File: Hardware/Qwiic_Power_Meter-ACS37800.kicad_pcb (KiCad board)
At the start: 4 copper layers, 30.5 x 38.1 mm, 55 parts, among them J1 Conn_01x01, J10 Conn_01x01, J11 Conn_01x01, J2 Conn_01x04, J3 Qwiic_RA, J4 HI, J5 LO, J6 Conn_01x01, J7 Qwiic_RA, J8 Conn_01x01, J9 Conn_01x01, U1 ACS37800

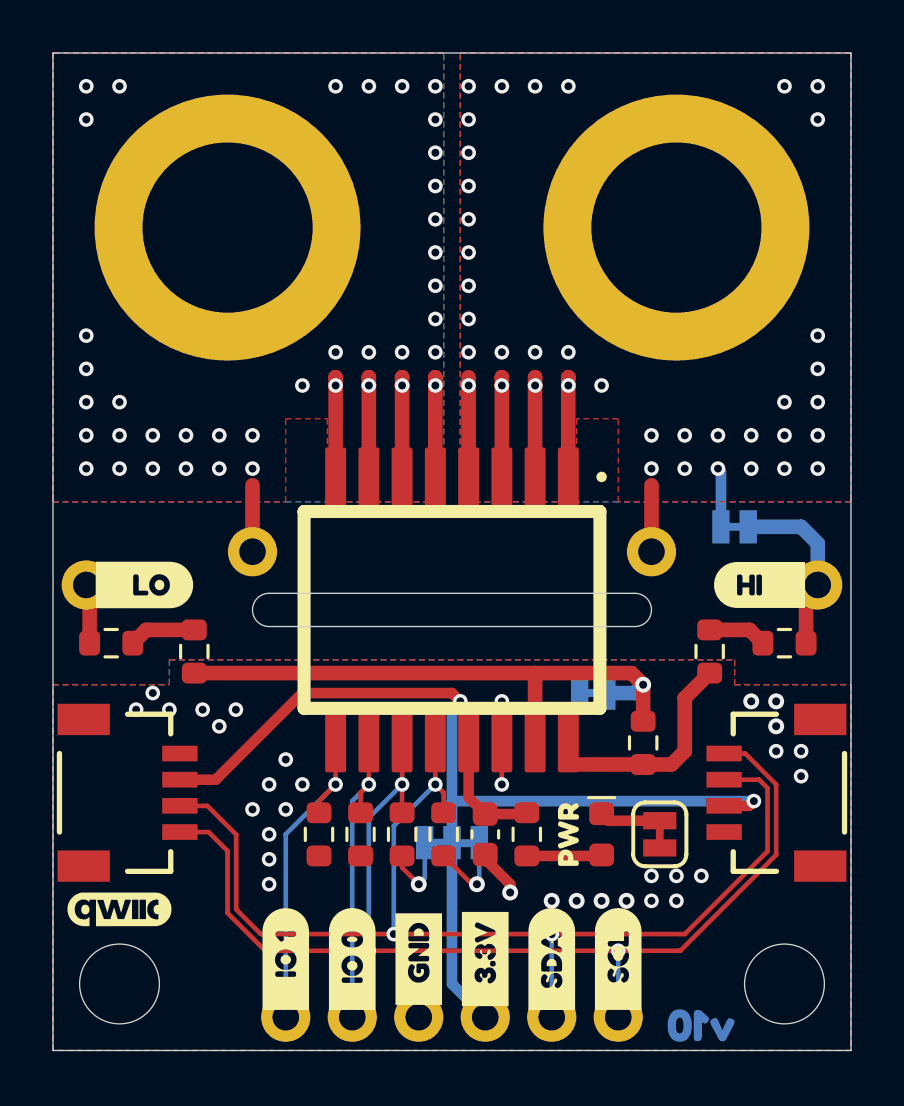
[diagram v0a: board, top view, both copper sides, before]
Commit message: Add missing fiducials
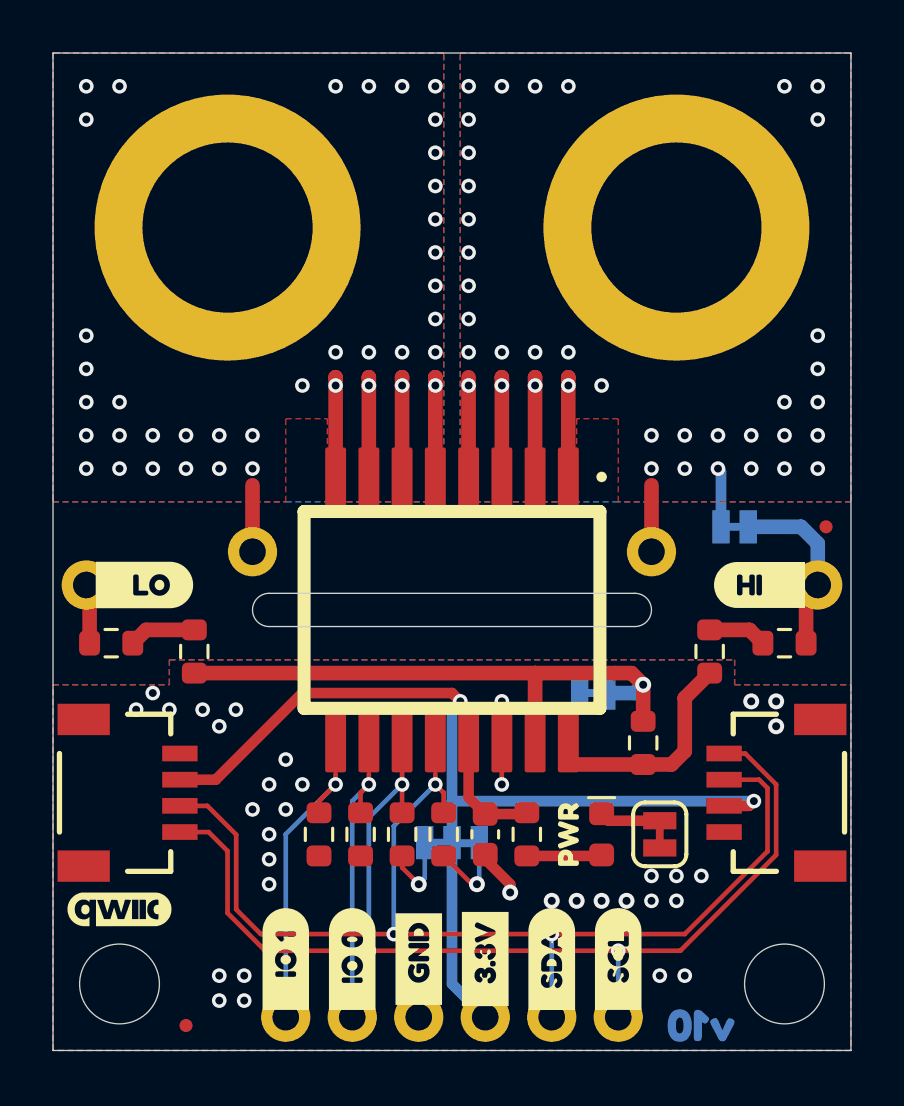
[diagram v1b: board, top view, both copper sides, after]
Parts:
- added Ref**: Fiducial_0.5mm_Mask1mm, SparkFun-Aesthetic:Fiducial_0.5mm_Mask1mm, F.Cu at (152.4, 95.9)
- added Ref**: Fiducial_0.5mm_Mask1mm, SparkFun-Aesthetic:Fiducial_0.5mm_Mask1mm, F.Cu at (128.0, 114.9)
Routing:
- net GND: vias 29 -> 35
- net (no net): vias 3 -> 0
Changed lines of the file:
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@@
 		(tags "kb_params=eyJBbGlnbm1lbnRDaG9pY2UiOiAiUmlnaHQiLCAiQ2FwTGVmdENob2ljZSI6ICJbIiwgIkNhcFJpZ2h0Q2hvaWNlIjogIl0iLCAiRm9udENvbWJvQm94IjogIkZyZWRkeVNwYXJrLVJlZ3VsYXIiLCAiSGVpZ2h0Q3RybCI6IDAuOCwgIkxheWVyQ29tYm9Cb3giOiAiRi5TaWxrUyIsICJMaW5lU3BhY2luZ0N0cmwiOiAxLjAsICJNdWx0aUxpbmVUZXh0IjogIlBXUiIsICJQYWRkaW5nQm90dG9tQ3RybCI6IDUuMCwgIlBhZGRpbmdMZWZ0Q3RybCI6IDUuMCwgIlBhZGRpbmdSaWdodEN0cmwiOiAwLjAsICJQYWRkaW5nVG9wQ3RybCI6IDUuMCwgIldpZHRoQ3RybCI6IDMuMCwgImFkdmFuY2VkQ2hlY2tib3giOiB0cnVlLCAiaW5saW5lRm9ybWF0VGV4dGJveCI6IHRydWUsICJsaW5lb3ZlclN0eWxlQ2hvaWNlIjogIlNxdWFyZSIsICJsaW5lb3ZlclRoaWNrbmVzc0N0cmwiOiAxfQ==")
 		(property "Reference" "kibuzzard-67B80BA2"
-			(at 0 -3.459445 270)
+			(at 0 -3.459445 -90)
 			(layer "F.SilkS")
 			(hide yes)
@@
 		)
 		(property "Value" "G***"
-			(at 0 3.459445 270)
+			(at 0 3.459445 -90)
 			(layer "F.SilkS")
 			(hide yes)
@@
 		)
 	)
+	(footprint "SparkFun-Aesthetic:Fiducial_0.5mm_Mask1mm"
+		(layer "F.Cu")
+		(at 152.4 95.885)
+		(descr "Circular Fiducial, 0.5mm bare copper, 1mm soldermask opening (Level C)")
+		(tags "SparkFun fiducial")
+		(property "Reference" "Ref**"
+			(at 0 -1.5 0)
+			(layer "F.Fab")
+			(effects
+				(font
+					(size 0.5 0.5)
+					(thickness 0.1)
+				)
+			)
+		)
+		(property "Value" "Fiducial_0.5mm_Mask1mm"
+			(at 0 1.5 0)
+			(layer "F.Fab")
+			(effects
+				(font
+					(size 0.5 0.5)
+					(thickness 0.1)
+				)
+			)
+		)
+		(property "Footprint" "SparkFun-Aesthetic:Fiducial_0.5mm_Mask1mm"
+			(at 0 0 0)
+			(unlocked yes)
+			(layer "F.Fab")
+			(hide yes)
+			(effects
+				(font
+					(size 1.27 1.27)
+				)
+			)
+		)
+		(property "Datasheet" ""
+			(at 0 0 0)
+			(unlocked yes)
+			(layer "F.Fab")
+			(hide yes)
+			(effects
+				(font
+					(size 1.27 1.27)
+				)
+			)
+		)
+		(property "Description" ""
+			(at 0 0 0)
+			(unlocked yes)
+			(layer "F.Fab")
+			(hide yes)
+			(effects
+				(font
+					(size 1.27 1.27)
+				)
+			)
+		)
+		(attr smd)
+		(fp_circle
+			(center 0 0)
+			(end 0.75 0)
+			(stroke
+				(width 0.05)
+				(type solid)
+			)
+			(fill none)
+			(layer "F.CrtYd")
+		)
+		(fp_circle
+			(center 0 0)
+			(end 0.5 0)
+			(stroke
+				(width 0.1)
+				(type solid)
+			)
+			(fill none)
+			(layer "F.Fab")
+		)
+		(pad "" smd circle
+			(at 0 0)
+			(size 0.5 0.5)
+			(layers "F.Cu" "F.Mask")
+			(clearance 0.25)
+		)
+	)
 	(footprint "SparkFun-Resistor:R_0603_1608Metric"
 		(layer "F.Cu")
@@
 		)
 	)
+	(footprint "SparkFun-Aesthetic:Fiducial_0.5mm_Mask1mm"
+		(layer "F.Cu")
+		(at 127.9525 114.935)
+		(descr "Circular Fiducial, 0.5mm bare copper, 1mm soldermask opening (Level C)")
+		(tags "SparkFun fiducial")
+		(property "Reference" "Ref**"
+			(at 0 -1.5 0)
+			(layer "F.Fab")
+			(effects
+				(font
+					(size 0.5 0.5)
+					(thickness 0.1)
+				)
+			)
+		)
+		(property "Value" "Fiducial_0.5mm_Mask1mm"
+			(at 0 1.5 0)
+			(layer "F.Fab")
+			(effects
+				(font
+					(size 0.5 0.5)
+					(thickness 0.1)
+				)
+			)
+		)
+		(property "Footprint" "SparkFun-Aesthetic:Fiducial_0.5mm_Mask1mm"
+			(at 0 0 0)
+			(unlocked yes)
+			(layer "F.Fab")
+			(hide yes)
+			(effects
+				(font
+					(size 1.27 1.27)
+				)
+			)
+		)
+		(property "Datasheet" ""
+			(at 0 0 0)
+			(unlocked yes)
+			(layer "F.Fab")
+			(hide yes)
+			(effects
+				(font
+					(size 1.27 1.27)
+				)
+			)
+		)
+		(property "Description" ""
+			(at 0 0 0)
+			(unlocked yes)
+			(layer "F.Fab")
+			(hide yes)
+			(effects
+				(font
+					(size 1.27 1.27)
+				)
+			)
+		)
+		(attr smd)
+		(fp_circle
+			(center 0 0)
+			(end 0.75 0)
+			(stroke
+				(width 0.05)
+				(type solid)
+			)
+			(fill none)
+			(layer "F.CrtYd")
+		)
+		(fp_circle
+			(center 0 0)
+			(end 0.5 0)
+			(stroke
+				(width 0.1)
+				(type solid)
+			)
+			(fill none)
+			(layer "F.Fab")
+		)
+		(pad "" smd circle
+			(at 0 0)
+			(size 0.5 0.5)
+			(layers "F.Cu" "F.Mask")
+			(clearance 0.25)
+		)
+	)
 	(footprint "SparkFun-Connector:1x01"
 		(layer "F.Cu")
@@
 		(layer "Edge.Cuts")
 	)
-	(via
-		(at 151.4475 104.4575)
-		(size 0.56)
-		(drill 0.3)
-		(layers "F.Cu" "B.Cu")
-		(net 0)
-	)
-	(via
-		(at 151.4475 105.41)
-		(size 0.56)
-		(drill 0.3)
-		(layers "F.Cu" "B.Cu")
-		(net 0)
-	)
-	(via
-		(at 150.495 104.4575)
-		(size 0.56)
-		(drill 0.3)
-		(layers "F.Cu" "B.Cu")
-		(net 0)
-	)
 	(segment
 		(start 139.3825 108.585)
@@
 	)
 	(via
+		(at 129.2225 113.9825)
+		(size 0.56)
+		(drill 0.3)
+		(layers "F.Cu" "B.Cu")
+		(free yes)
+		(net 1)
+	)
+	(via
 		(at 126.0475 102.87)
 		(size 0.56)
@@
 	)
 	(via
+		(at 147.0025 113.03)
+		(size 0.56)
+		(drill 0.3)
+		(layers "F.Cu" "B.Cu")
+		(free yes)
+		(net 1)
+	)
+	(via
 		(at 146.685 110.1725)
 		(size 0.56)
@@
 	)
 	(via
+		(at 129.2225 113.03)
+		(size 0.56)
+		(drill 0.3)
+		(layers "F.Cu" "B.Cu")
+		(free yes)
+		(net 1)
+	)
+	(via
+		(at 130.175 113.03)
+		(size 0.56)
+		(drill 0.3)
+		(layers "F.Cu" "B.Cu")
+		(free yes)
+		(net 1)
+	)
+	(via
 		(at 131.7625 106.68)
 		(size 0.56)
@@
 	)
 	(via
+		(at 146.05 113.03)
+		(size 0.56)
+		(drill 0.3)
+		(layers "F.Cu" "B.Cu")
+		(free yes)
+		(net 1)
+	)
+	(via
 		(at 145.7325 109.22)
 		(size 0.56)
@@
 		(size 0.56)
 		(drill 0.3)
+		(layers "F.Cu" "B.Cu")
+		(free yes)
+		(net 1)
+	)
+	(via
+		(at 130.175 113.9825)
+		(size 0.56)
+		(drill 0.3)

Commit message: Update SOIC Wide footprint
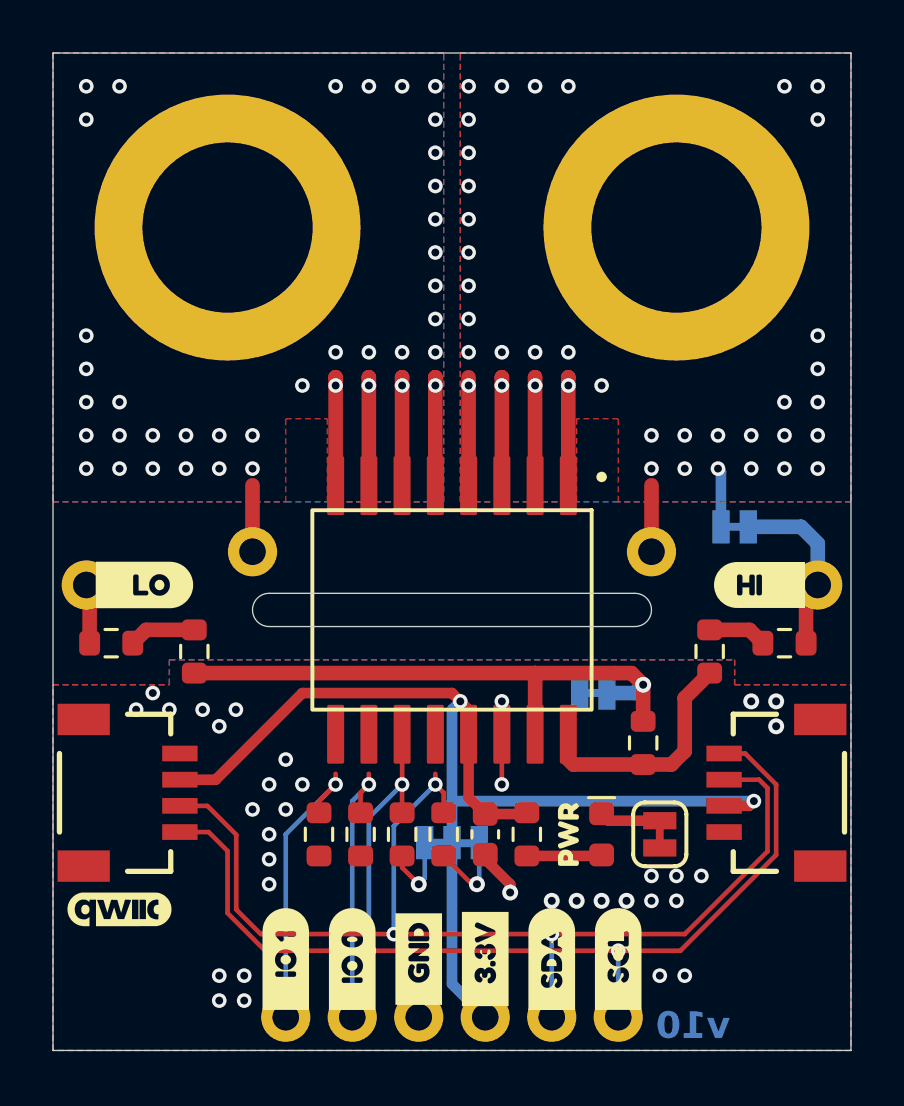
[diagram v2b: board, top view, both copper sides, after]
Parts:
- removed REF** (x2): STAND-OFF-TIGHT, SparkFun-Hardware:Standoff_Tight
- removed the Ref** at (152.4, 95.9)
- removed the Ref** at (128.0, 114.9)
- removed kibuzzard-67B81202: G***, kibuzzard-67B81202
- added G1: OSHW_Logo, SparkFun-Aesthetic:Creative_Commons_License, F.Cu at (233.0, 163.5)
- J3, J7: footprint SparkFun-Connector:JST_SMD_1.0mm-4_RA -> SparkFun-Connector:JST_SMD_1.0mm-4_Black
- J4: value HI -> Conn_01x01
- J5: value LO -> Conn_01x01
- J8, J9: footprint SparkFun-Connector:1x01_0.4 -> SparkFun-Connector:1x01_0.4in
- JP3: value IP+ -> ~
- JP4: value VINN -> ~
- U1: footprint SparkFun-Semiconductor-Standard:SO-16_WIDE_POWER -> SparkFun-Semiconductor-Standard:SO-16_Wide_Power
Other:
- board text added: "v10"

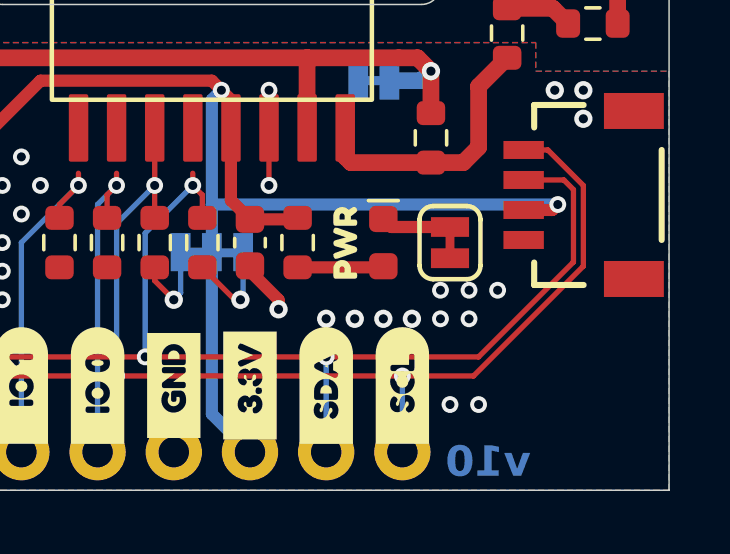
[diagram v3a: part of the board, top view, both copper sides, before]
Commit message: Adds measures, labels LED jumper, updates some schematic text
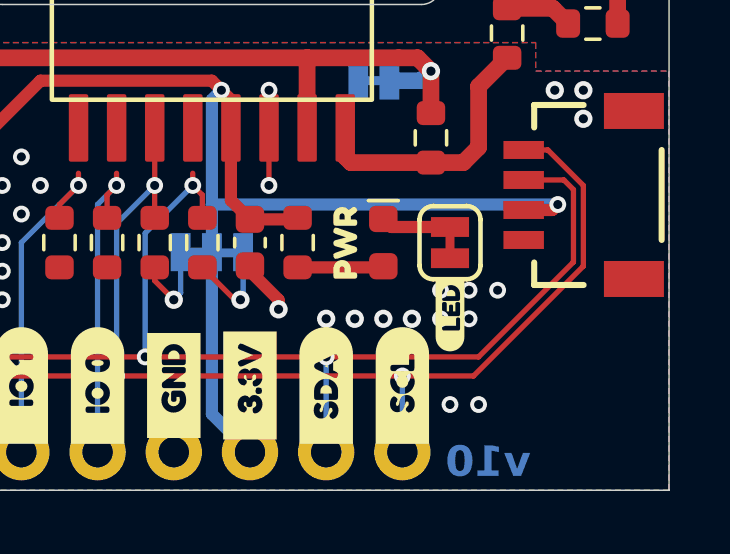
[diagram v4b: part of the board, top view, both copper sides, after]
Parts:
- removed J2: Conn_01x04, SparkFun-Connector:1x04
- added J12: I2C, SparkFun-Connector:1x04, F.Cu at (136.8, 114.6)
- added kibuzzard-681260C2: G***, kibuzzard-681260C2, F.Cu at (146.1, 110.0)
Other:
- copper layers 4 -> 2
